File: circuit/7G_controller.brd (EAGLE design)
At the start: 66.3 x 72 mm, 19 parts, among them Q1 3.6864MHz

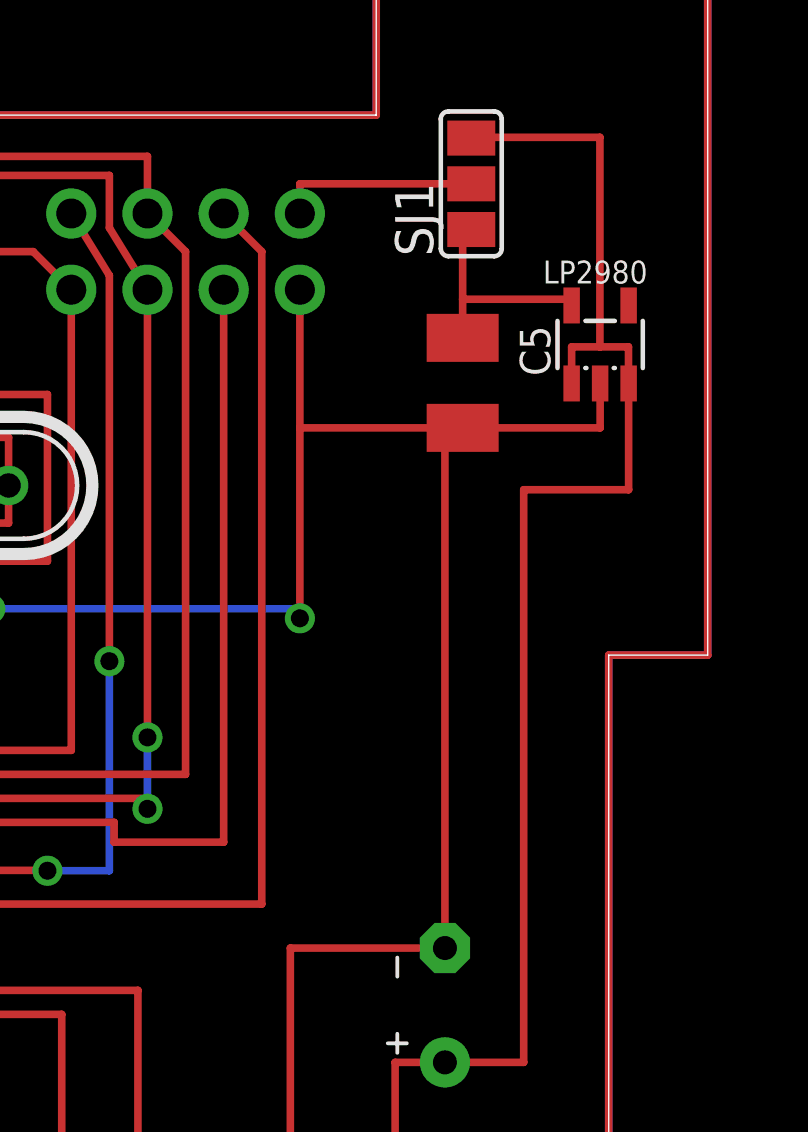
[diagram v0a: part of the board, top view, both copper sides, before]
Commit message: 
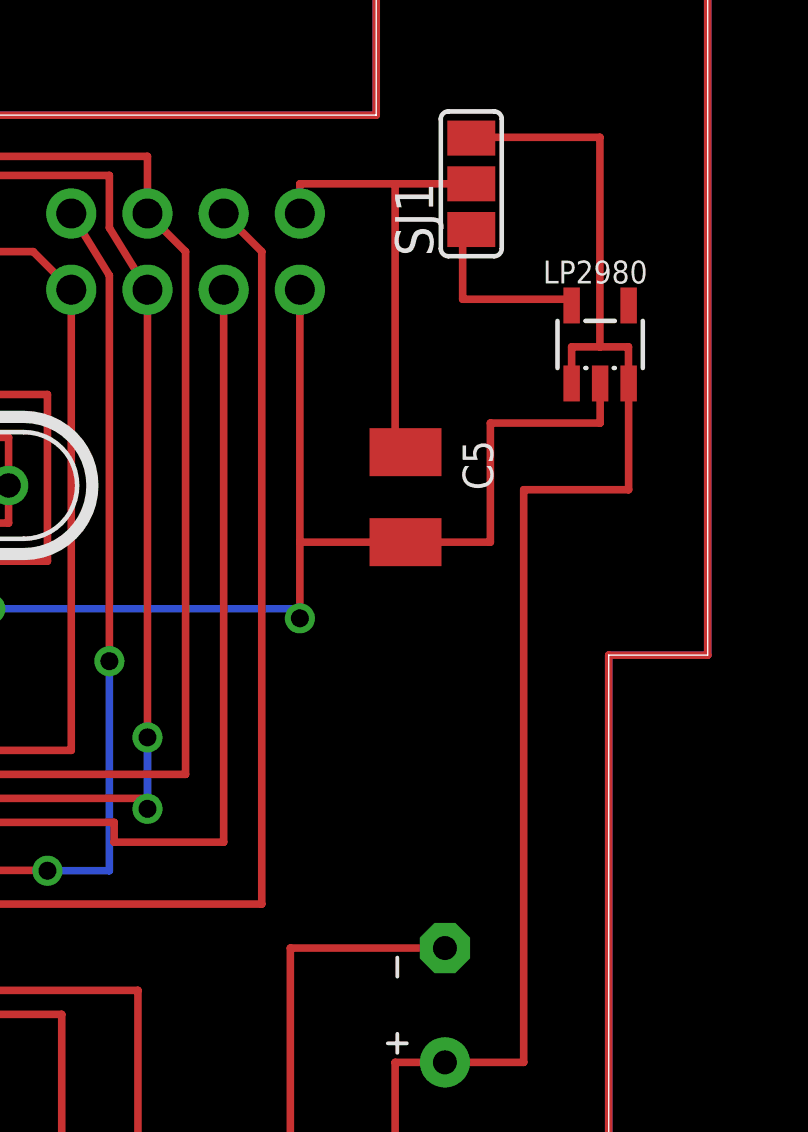
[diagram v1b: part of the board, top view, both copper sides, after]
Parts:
- moved C5 4.26 mm to (56.2, 36.3)
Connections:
- new net AREF: ATMEGA169PV.62
- net N$5: no longer C5.+
- net N$6: now also C5.+
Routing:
- net GND: track 200.9 -> 187.4 mm
- net N$6: track 6.70 -> 16.0 mm
- net N$5: track 7.74 -> 6.45 mm
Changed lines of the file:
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@@
 <attribute name="OC_FARNELL" value="unknown" x="48.5775" y="7.62" size="1.778" layer="27" display="off"/>
 </element>
-<element name="C5" library="rcl" package="SMC_B" value="1uF" x="58.13125" y="40.075" rot="R270"/>
+<element name="C5" library="rcl" package="SMC_B" value="1uF" x="56.22625" y="36.265" rot="R270"/>
 <element name="R2" library="rcl" package="R0805" value="470R" x="15.9512" y="53.11" rot="R90"/>
 <element name="R3" library="rcl" package="R0805" value="470R" x="11.9825" y="53.1075" rot="R90"/>
@@
 <contactref element="LP2980" pad="2"/>
 <contactref element="UART" pad="GND"/>
-<contactref element="C5" pad="-"/>
 <contactref element="AVR_ISP" pad="GND"/>
 <contactref element="AVR_JTAG" pad="P$10"/>
@@
 <wire x1="31.115" y1="60.6425" x2="35.40125" y2="60.6425" width="0.254" layer="1"/>
 <wire x1="35.40125" y1="42.70125" x2="37.62375" y2="42.70125" width="0.254" layer="1"/>
-<wire x1="52.705" y1="43.18" x2="52.705" y2="38.575" width="0.254" layer="1"/>
-<wire x1="52.705" y1="38.575" x2="57.54" y2="38.575" width="0.254" layer="1"/>
-<wire x1="57.54" y1="38.575" x2="58.13125" y2="38.575" width="0.254" layer="1"/>
-<wire x1="62.71375" y1="40.055" x2="62.71375" y2="38.575" width="0.254" layer="1"/>
-<wire x1="62.71375" y1="38.575" x2="58.13125" y2="38.575" width="0.254" layer="1"/>
+<wire x1="62.71375" y1="40.055" x2="62.71375" y2="38.735" width="0.254" layer="1"/>
+<wire x1="62.71375" y1="38.735" x2="62.71375" y2="38.575" width="0" layer="19" extent="1-16"/>
 <wire x1="35.53875" y1="13.335" x2="33.79" y2="13.335" width="0.254" layer="1"/>
 <wire x1="33.79" y1="13.335" x2="33.79" y2="16.425" width="0.254" layer="1"/>
@@
 <wire x1="25.79" y1="18.415" x2="25.79" y2="16.425" width="0.254" layer="1"/>
 <wire x1="52.3875" y1="7.62" x2="52.3875" y2="21.235" width="0.254" layer="1"/>
-<wire x1="57.54" y1="21.235" x2="57.54" y2="38.575" width="0.254" layer="1"/>
 <wire x1="57.54" y1="21.235" x2="52.3875" y2="21.235" width="0.254" layer="1"/>
 <wire x1="30.59" y1="32.025" x2="30.63875" y2="32.025" width="0.254" layer="1"/>
@@
 <wire x1="39.0525" y1="39.6875" x2="39.0525" y2="42.70125" width="0.254" layer="1"/>
 <wire x1="39.0525" y1="42.70125" x2="37.62375" y2="42.70125" width="0.254" layer="1"/>
-<wire x1="52.705" y1="38.575" x2="52.705" y2="32.22625" width="0.254" layer="1"/>
+<wire x1="52.705" y1="43.18" x2="52.705" y2="34.765" width="0.254" layer="1"/>
 <via x="52.705" y="32.22625" extent="1-16" drill="0.6" shape="square"/>
+<wire x1="52.705" y1="34.765" x2="52.705" y2="32.22625" width="0.254" layer="1"/>
 <wire x1="52.705" y1="32.22625" x2="52.705" y2="32.54375" width="0.254" layer="16"/>
 <wire x1="52.705" y1="32.54375" x2="42.38625" y2="32.54375" width="0.254" layer="16"/>
@@
 <wire x1="27.94" y1="57.785" x2="35.40125" y2="57.785" width="0.254" layer="1"/>
 <wire x1="20.955" y1="65.0875" x2="20.955" y2="58.42" width="0.254" layer="1"/>
+<contactref element="C5" pad="-"/>
+<wire x1="56.22625" y1="34.765" x2="52.705" y2="34.765" width="0.254" layer="1"/>
+<wire x1="56.22625" y1="34.765" x2="59.055" y2="34.765" width="0.254" layer="1"/>
+<wire x1="59.055" y1="34.765" x2="59.055" y2="38.735" width="0.254" layer="1"/>
+<wire x1="59.055" y1="38.735" x2="62.71375" y2="38.735" width="0.254" layer="1"/>
+<wire x1="52.705" y1="32.22625" x2="52.3875" y2="21.235" width="0" layer="19" extent="1-1"/>
 </signal>
 <signal name="MOSI">
@@
 <contactref element="NRF24L01" pad="+3.3V"/>
 <contactref element="SJ1" pad="2"/>
-<wire x1="58.41875" y1="46.71" x2="52.705" y2="46.71" width="0.254" layer="1"/>
+<wire x1="58.41875" y1="46.71" x2="55.88" y2="46.71" width="0.254" layer="1"/>
+<wire x1="55.88" y1="46.71" x2="52.705" y2="46.71" width="0.254" layer="1"/>
 <wire x1="52.705" y1="46.71" x2="52.705" y2="45.72" width="0.254" layer="1"/>
+<contactref element="C5" pad="+"/>
+<wire x1="56.22625" y1="37.765" x2="55.88" y2="37.765" width="0.4064" layer="1"/>
+<wire x1="55.88" y1="37.765" x2="55.88" y2="46.71" width="0.254" layer="1"/>
 </signal>
 <signal name="LEDSCRL">
@@
 <contactref element="SJ1" pad="1"/>
 <contactref element="LP2980" pad="5"/>
-<contactref element="C5" pad="+"/>
-<wire x1="58.13125" y1="41.575" x2="58.13125" y2="42.8625" width="0.254" layer="1"/>
 <wire x1="58.13125" y1="42.8625" x2="58.13125" y2="45.186" width="0.254" layer="1"/>
 <wire x1="58.13125" y1="45.186" x2="58.41875" y2="45.186" width="0.254" layer="1"/>
@@
 </polygon>
 </signal>
+<signal name="AREF">
+<contactref element="ATMEGA169PV" pad="62"/>
+</signal>
 </signals>

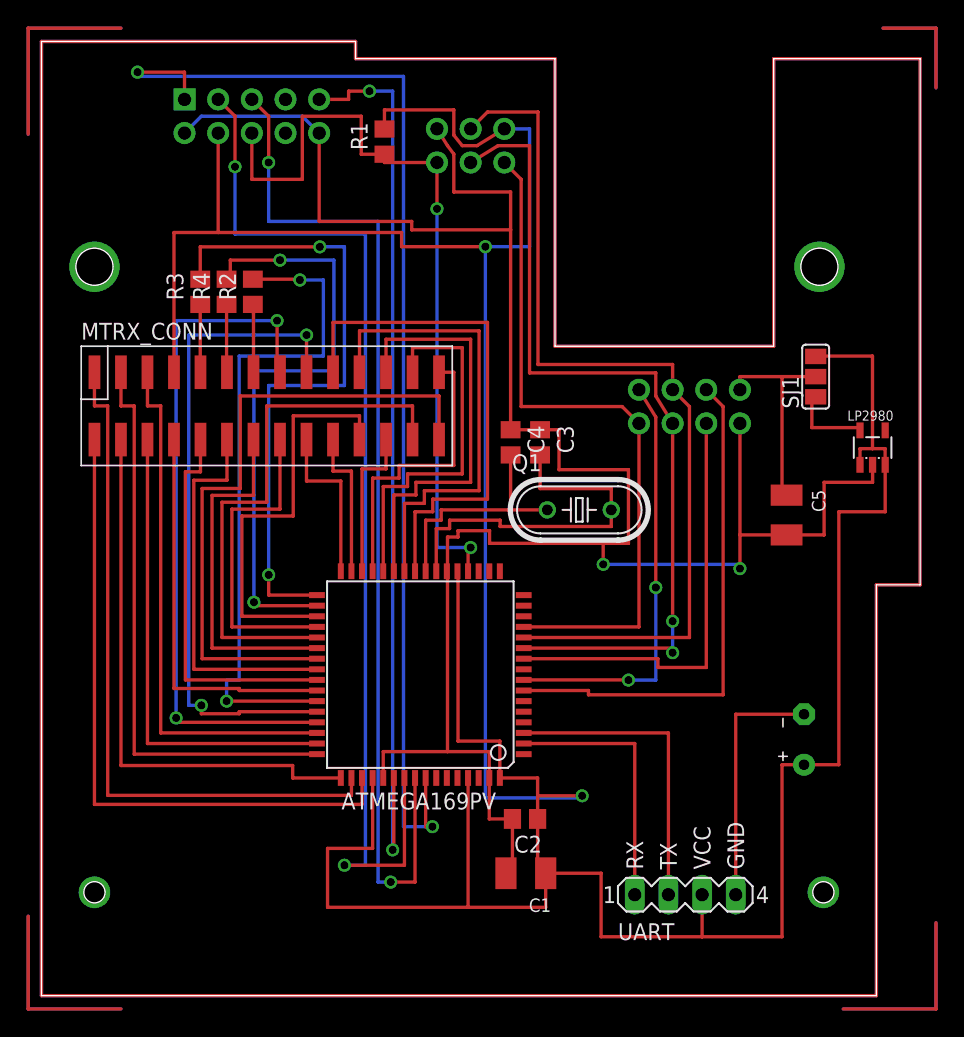
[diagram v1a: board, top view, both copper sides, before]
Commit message: 
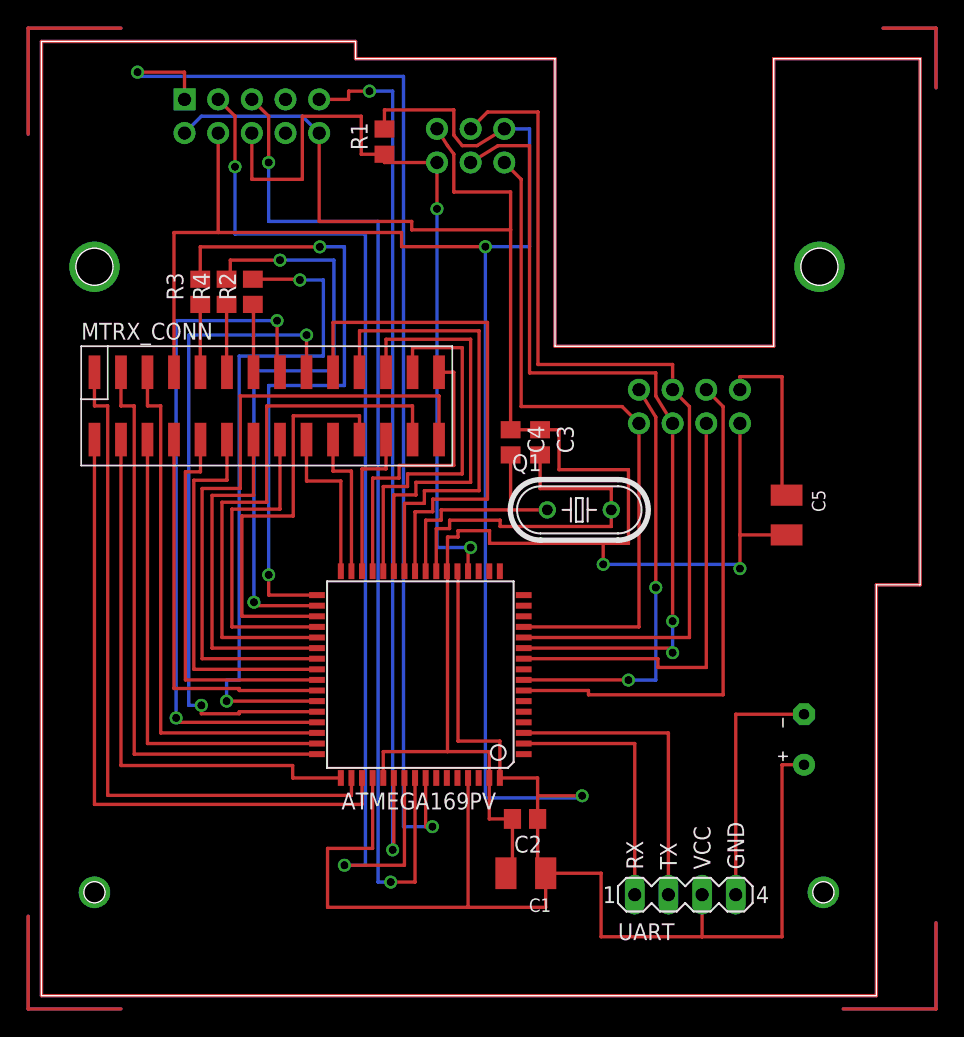
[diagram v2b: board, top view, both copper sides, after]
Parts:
- removed LP2980: LP2980, KileParts:SOT25
- removed SJ1: (no value), jumper:SJ_2
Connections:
- removed net N$5: LP2980.5, SJ1.1
- removed net N$6: C5.+, NRF24L01.+3.3V, SJ1.2
- net GND: no longer LP2980.2
- net VCC: now also C5.+, NRF24L01.+3.3V; no longer LP2980.1, LP2980.3, SJ1.3
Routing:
- net VCC: track 278.1 -> 247.1 mm
- net N$6: track 16.0 -> 0.00 mm
- net GND: track 187.4 -> 175.6 mm
- net N$5: track 6.45 -> 0.00 mm
- removed copper zone on layer 1, net N$4
- removed copper zone on layer 16, net N$4
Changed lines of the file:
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@@
 <element name="MTRX_CONN" library="KileParts" package="SS7G_CONN_SMD" value="SS7G_CONNSMD" x="17" y="44.5"/>
 <element name="BAT1" library="KileParts" package="BATTERY" value="" x="57.54" y="19.33" rot="R90"/>
-<element name="LP2980" library="KileParts" package="SOT25" value="LP2980" x="62.71375" y="41.355"/>
-<element name="SJ1" library="jumper" package="SJ_2" value="" x="58.41875" y="46.71" rot="R90"/>
 <element name="UART" library="KileParts" package="UART_PORT" value="" x="48.5775" y="7.62">
 <attribute name="OC_NEWARK" value="unknown" x="48.5775" y="7.62" size="1.778" layer="27" display="off"/>
@@
 <contactref element="MTRX_CONN" pad="4"/>
 <contactref element="ATMEGA169PV" pad="61"/>
-<contactref element="SJ1" pad="3"/>
-<contactref element="LP2980" pad="1"/>
-<contactref element="LP2980" pad="3"/>
 <contactref element="UART" pad="+5V"/>
 <contactref element="AVR_JTAG" pad="P$4"/>
@@
 <wire x1="25.88" y1="66.83375" x2="25.88" y2="65.39" width="0.254" layer="1"/>
 <wire x1="10" y1="47.04" x2="10" y2="57.58375" width="0.254" layer="1"/>
-<wire x1="61.76375" y1="40.055" x2="61.76375" y2="41.275" width="0.254" layer="1"/>
-<wire x1="61.76375" y1="41.275" x2="62.70625" y2="41.275" width="0.254" layer="1"/>
-<wire x1="62.70625" y1="41.275" x2="63.65875" y2="41.275" width="0.254" layer="1"/>
-<wire x1="63.65875" y1="41.275" x2="63.65875" y2="40.055" width="0.254" layer="1"/>
-<wire x1="63.65875" y1="40.055" x2="63.66375" y2="40.055" width="0.254" layer="1"/>
-<wire x1="58.41875" y1="48.234" x2="58.41875" y2="48.26" width="0.254" layer="1"/>
-<wire x1="58.41875" y1="48.26" x2="62.70625" y2="48.26" width="0.254" layer="1"/>
-<wire x1="62.70625" y1="48.26" x2="62.70625" y2="41.275" width="0.254" layer="1"/>
-<wire x1="57.54" y1="17.425" x2="60.16625" y2="17.425" width="0.254" layer="1"/>
-<wire x1="60.16625" y1="17.425" x2="60.16625" y2="36.5125" width="0.254" layer="1"/>
-<wire x1="60.16625" y1="36.5125" x2="63.66375" y2="36.5125" width="0.254" layer="1"/>
-<wire x1="63.66375" y1="36.5125" x2="63.66375" y2="40.055" width="0.254" layer="1"/>
 <wire x1="37.43875" y1="13.335" x2="37.43875" y2="15.08125" width="0.254" layer="1"/>
 <wire x1="37.43875" y1="15.08125" x2="37.43875" y2="16.425" width="0.254" layer="1"/>
@@
 <wire x1="27.175" y1="57.58375" x2="27.175" y2="56.515" width="0.254" layer="1"/>
 <wire x1="27.175" y1="56.515" x2="33.49625" y2="56.515" width="0.254" layer="1"/>
+<contactref element="NRF24L01" pad="+3.3V"/>
+<contactref element="C5" pad="+"/>
+<wire x1="55.88" y1="46.71" x2="52.705" y2="46.71" width="0.254" layer="1"/>
+<wire x1="52.705" y1="46.71" x2="52.705" y2="45.72" width="0.254" layer="1"/>
+<wire x1="56.22625" y1="37.765" x2="55.88" y2="37.765" width="0.4064" layer="1"/>
+<wire x1="55.88" y1="37.765" x2="55.88" y2="46.71" width="0.254" layer="1"/>
+<wire x1="36.83" y1="56.515" x2="52.705" y2="46.71" width="0" layer="19" extent="1-16"/>
 </signal>
 <signal name="GND">
@@
 <contactref element="C4" pad="1"/>
 <contactref element="BAT1" pad="-"/>
-<contactref element="LP2980" pad="2"/>
 <contactref element="UART" pad="GND"/>
 <contactref element="AVR_ISP" pad="GND"/>
@@
 <wire x1="31.115" y1="60.6425" x2="35.40125" y2="60.6425" width="0.254" layer="1"/>
 <wire x1="35.40125" y1="42.70125" x2="37.62375" y2="42.70125" width="0.254" layer="1"/>
-<wire x1="62.71375" y1="40.055" x2="62.71375" y2="38.735" width="0.254" layer="1"/>
-<wire x1="62.71375" y1="38.735" x2="62.71375" y2="38.575" width="0" layer="19" extent="1-16"/>
 <wire x1="35.53875" y1="13.335" x2="33.79" y2="13.335" width="0.254" layer="1"/>
 <wire x1="33.79" y1="13.335" x2="33.79" y2="16.425" width="0.254" layer="1"/>
@@
 <contactref element="C5" pad="-"/>
 <wire x1="56.22625" y1="34.765" x2="52.705" y2="34.765" width="0.254" layer="1"/>
-<wire x1="56.22625" y1="34.765" x2="59.055" y2="34.765" width="0.254" layer="1"/>
-<wire x1="59.055" y1="34.765" x2="59.055" y2="38.735" width="0.254" layer="1"/>
-<wire x1="59.055" y1="38.735" x2="62.71375" y2="38.735" width="0.254" layer="1"/>
 <wire x1="52.705" y1="32.22625" x2="52.3875" y2="21.235" width="0" layer="19" extent="1-1"/>
 </signal>
@@
 <wire x1="23.1775" y1="68.25" x2="24.75" y2="68.25" width="0.254" layer="1"/>
 </signal>
-<signal name="N$6">
-<contactref element="NRF24L01" pad="+3.3V"/>
-<contactref element="SJ1" pad="2"/>
-<wire x1="58.41875" y1="46.71" x2="55.88" y2="46.71" width="0.254" layer="1"/>
-<wire x1="55.88" y1="46.71" x2="52.705" y2="46.71" width="0.254" layer="1"/>
-<wire x1="52.705" y1="46.71" x2="52.705" y2="45.72" width="0.254" layer="1"/>
-<contactref element="C5" pad="+"/>
-<wire x1="56.22625" y1="37.765" x2="55.88" y2="37.765" width="0.4064" layer="1"/>
-<wire x1="55.88" y1="37.765" x2="55.88" y2="46.71" width="0.254" layer="1"/>
-</signal>
 <signal name="LEDSCRL">
 <contactref element="MTRX_CONN" pad="5"/>
@@
 <wire x1="16" y1="47.04" x2="16" y2="51.4575" width="0.254" layer="1"/>
 <wire x1="16" y1="51.4575" x2="15.9512" y2="52.16" width="0.254" layer="1"/>
-</signal>
-<signal name="N$5">
-<contactref element="SJ1" pad="1"/>
-<contactref element="LP2980" pad="5"/>
-<wire x1="58.13125" y1="42.8625" x2="58.13125" y2="45.186" width="0.254" layer="1"/>
-<wire x1="58.13125" y1="45.186" x2="58.41875" y2="45.186" width="0.254" layer="1"/>
-<wire x1="61.76375" y1="42.655" x2="61.76375" y2="42.8625" width="0.254" layer="1"/>
-<wire x1="61.76375" y1="42.8625" x2="58.13125" y2="42.8625" width="0.254" layer="1"/>
 </signal>
 <signal name="N$29">
@@
 <wire x1="41.275" y1="23.025" x2="36.39" y2="23.025" width="0.254" layer="1"/>
 </signal>
-<signal name="N$4">
-<polygon width="0.254" layer="16" isolate="0.8128">
-<vertex x="0" y="0"/>
-<vertex x="63" y="0"/>
-<vertex x="63" y="31"/>
-<vertex x="66.3" y="31"/>
-<vertex x="66.3" y="70.7"/>
-<vertex x="55.25" y="70.7"/>
-<vertex x="55.25" y="49"/>
-<vertex x="38.75" y="49"/>
-<vertex x="38.75" y="70.7"/>
-<vertex x="23.7" y="70.7"/>
-<vertex x="23.7" y="72"/>
-<vertex x="0" y="72"/>
-</polygon>
-<polygon width="0.254" layer="1" isolate="0.8128">
-<vertex x="0" y="0"/>
-<vertex x="63" y="0"/>
-<vertex x="63" y="31"/>
-<vertex x="66.3" y="31"/>
-<vertex x="66.3" y="70.7"/>
-<vertex x="55.25" y="70.7"/>
-<vertex x="55.25" y="49"/>
-<vertex x="38.75" y="49"/>
-<vertex x="38.75" y="70.7"/>
-<vertex x="23.7" y="70.7"/>
-<vertex x="23.7" y="72"/>
-<vertex x="0" y="72"/>
-</polygon>
-</signal>
 <signal name="AREF">

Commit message: 
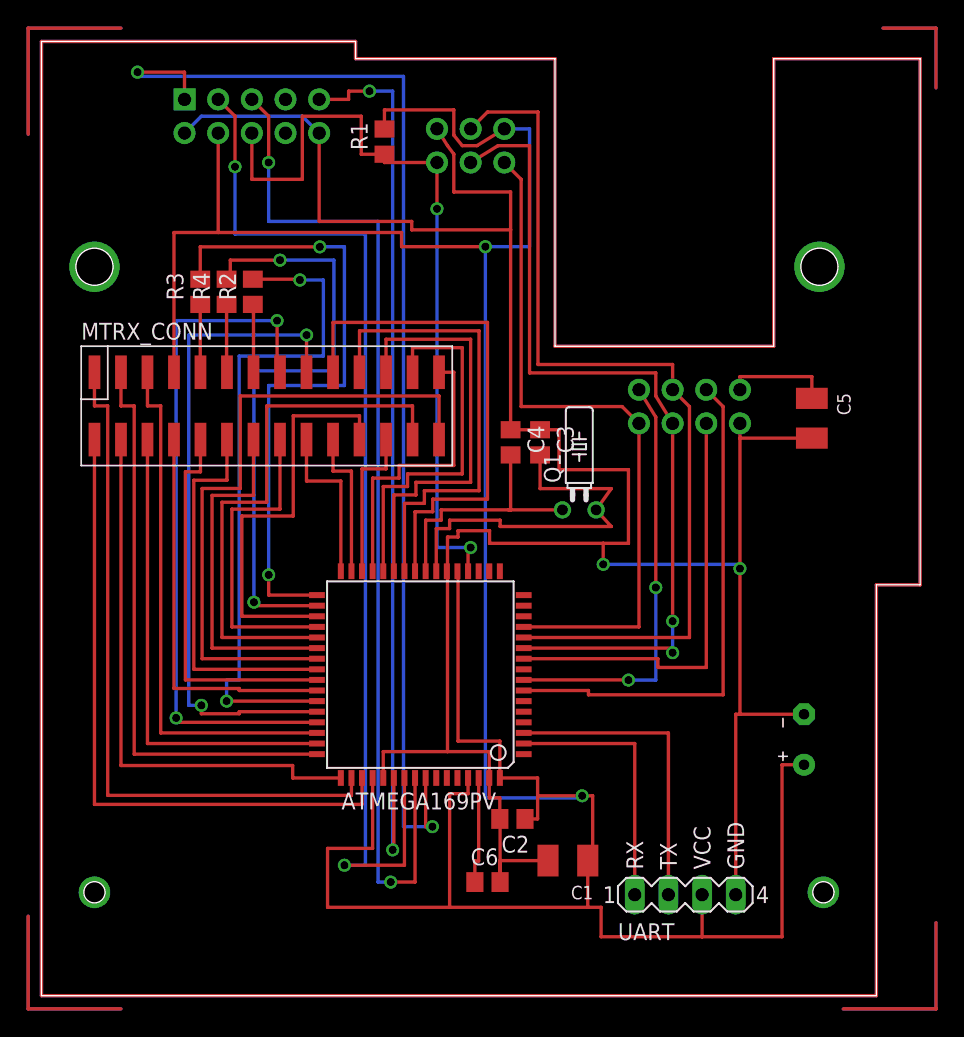
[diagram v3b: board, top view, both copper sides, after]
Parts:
- added C6: 100nF, rcl:C0805
- Q1: device SparkFun:HC49U-V -> crystal:TC26H
- moved C5 7.55 mm to (58.1, 43.6)
- moved C1 3.31 mm to (39.7, 10.2)
- moved C2 0.95 mm to (35.5, 13.3)
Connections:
- net AREF: now also C6.1
- net GND: now also C6.2
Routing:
- net GND: track 175.6 -> 193.4 mm
- net AREF: track 0.00 -> 8.14 mm
- net VCC: track 247.1 -> 244.3 mm
- net N$8: track 18.0 -> 19.1 mm
- net N$7: track 28.3 -> 29.1 mm
